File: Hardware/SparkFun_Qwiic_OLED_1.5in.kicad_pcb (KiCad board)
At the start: 2 copper layers, 34.3 x 48.3 mm, 72 parts, among them J1 Qwiic_RA, J2 Qwiic_RA, J4 Conn_01x24_FPC, J5 Conn_01x07, U2 WEO128128ASAP3N00000, U5 AP3012

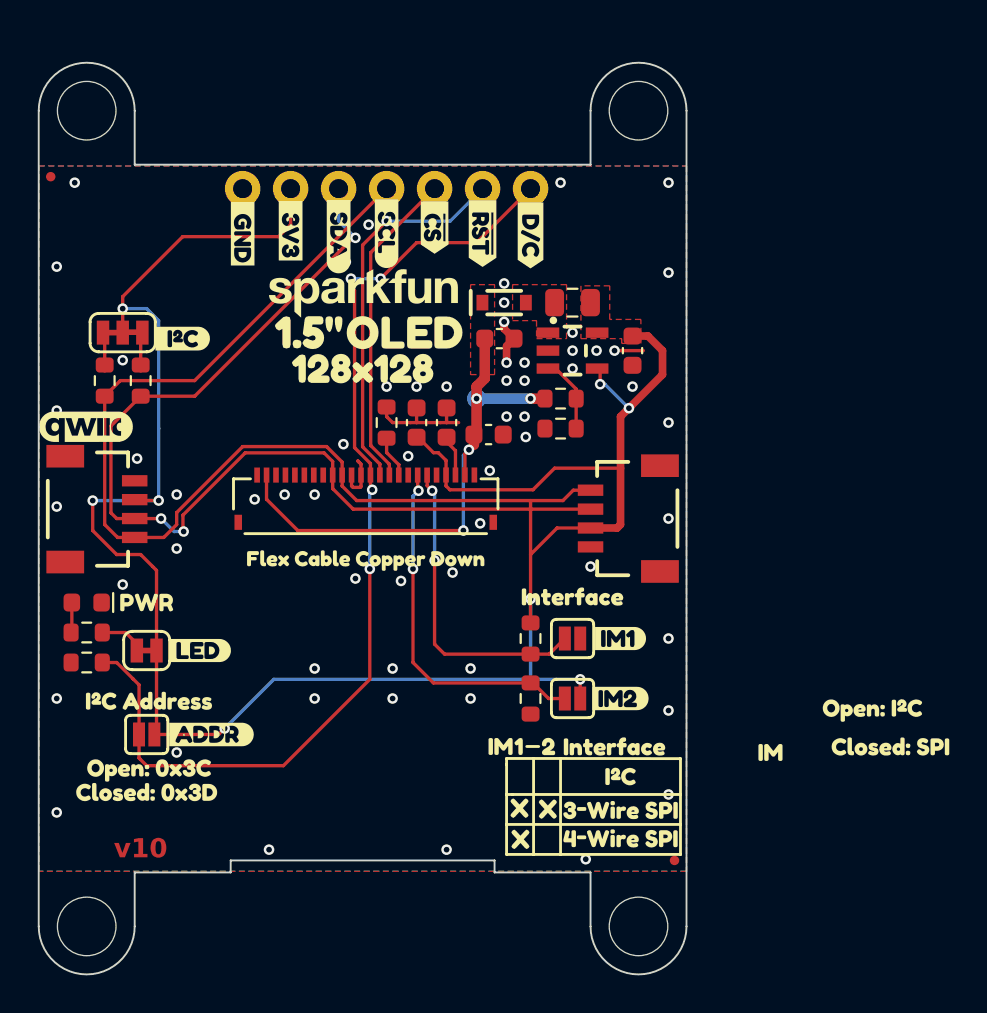
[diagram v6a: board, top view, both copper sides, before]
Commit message: Fixes the qwiic connectors being misaligned, updates measures
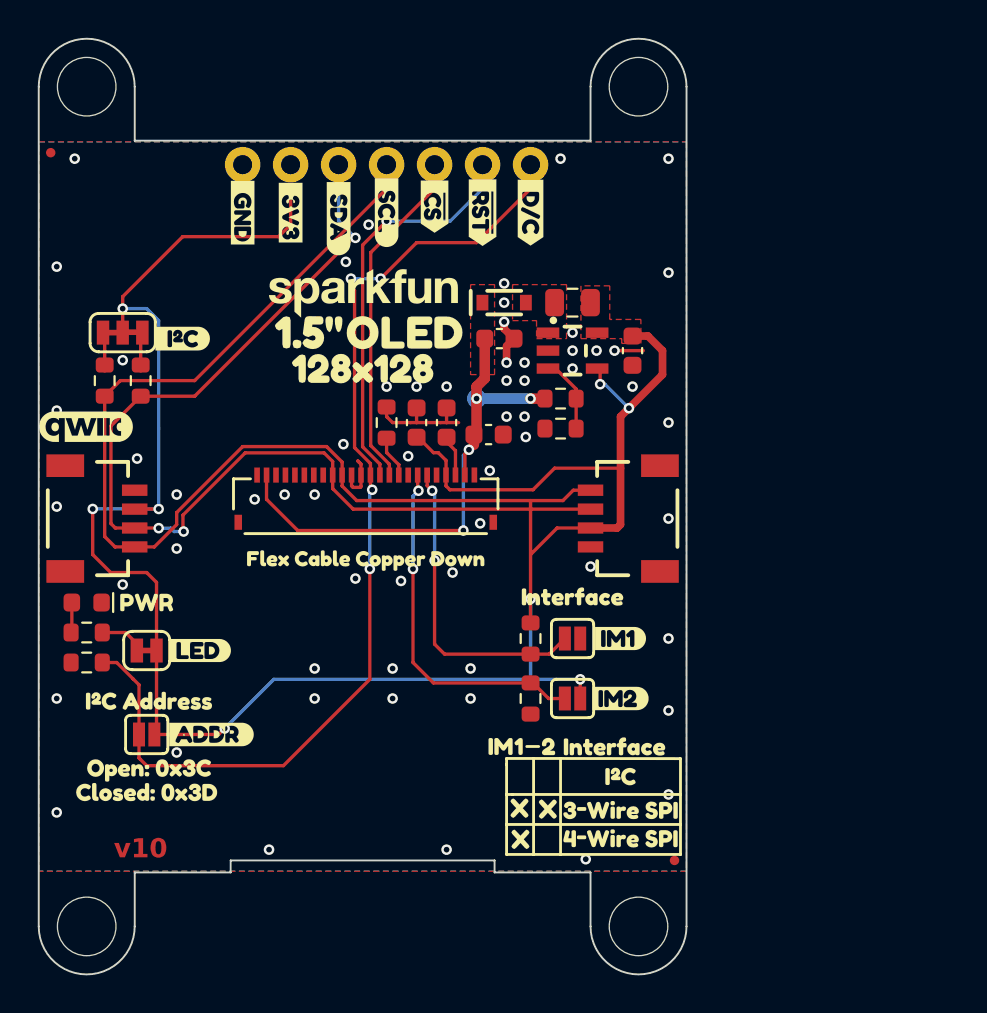
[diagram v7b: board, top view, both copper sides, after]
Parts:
- removed kibuzzard-680FCA02: G***, kibuzzard-680FCA02
- removed kibuzzard-680FCAD6: G***, kibuzzard-680FCAD6
- removed kibuzzard-68938227: G***, kibuzzard-68938227
- moved FID3 1.27 mm to (123.9, 67.3)
- moved J5 1.27 mm to (134.1, 67.9)
- moved ST1 1.27 mm to (125.8, 63.8)
- moved ST2 1.27 mm to (155.0, 63.8)
- moved kibuzzard-685B1775 1.21 mm to (149.3, 70.5)
- moved kibuzzard-67BF7EBF 1.11 mm to (134.1, 70.5)
- moved kibuzzard-67BF7F2F 1.11 mm to (141.7, 70.5)
- moved kibuzzard-680E7A4B 1.11 mm to (146.8, 70.5)
- moved kibuzzard-680E7A69 1.11 mm to (144.2, 70.2)
- moved kibuzzard-67BF7ED9 0.95 mm to (136.6, 70.5)
- moved kibuzzard-67BF7F13 0.95 mm to (139.1, 70.8)
- moved J2 0.50 mm to (128.3, 86.7)
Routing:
- net SCL/SCK: track 56.8 -> 57.6 mm
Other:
- board size 34.3 x 48.3 mm -> 34.3 x 49.5 mm

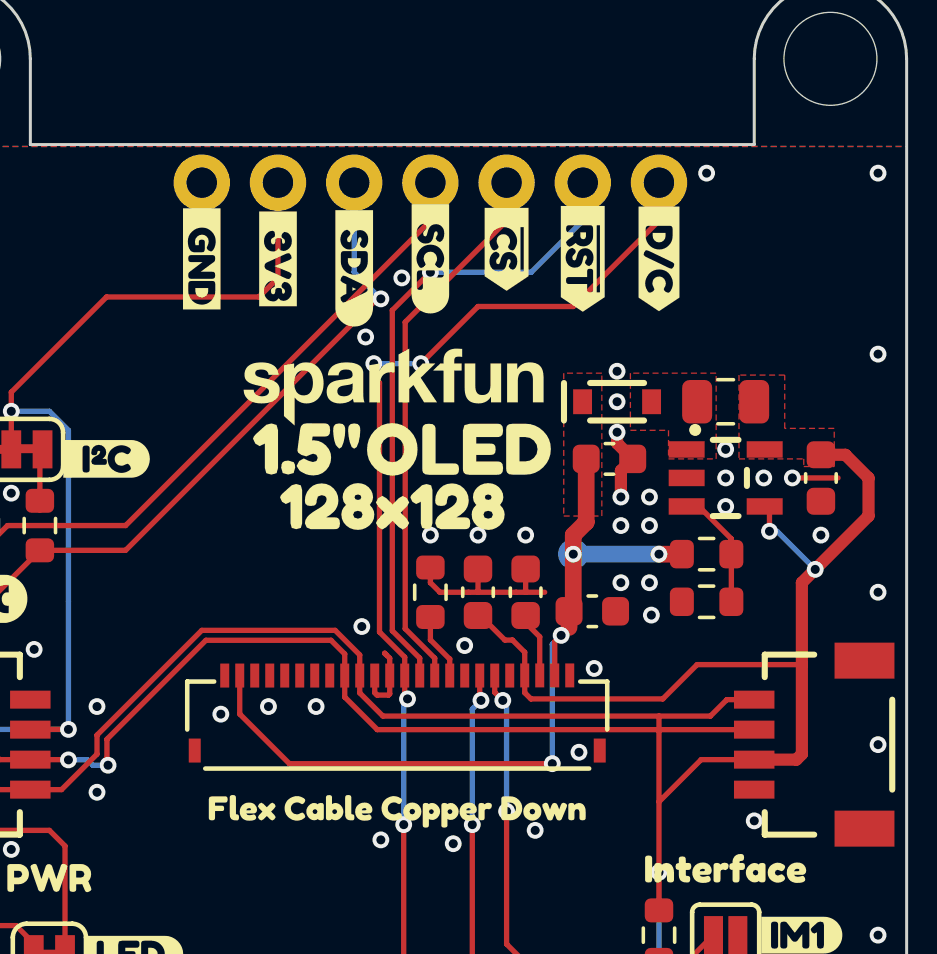
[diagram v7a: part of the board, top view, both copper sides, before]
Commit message: Increases the size of the board by .05", moves the FPC connector over .0065" so that it's in the center
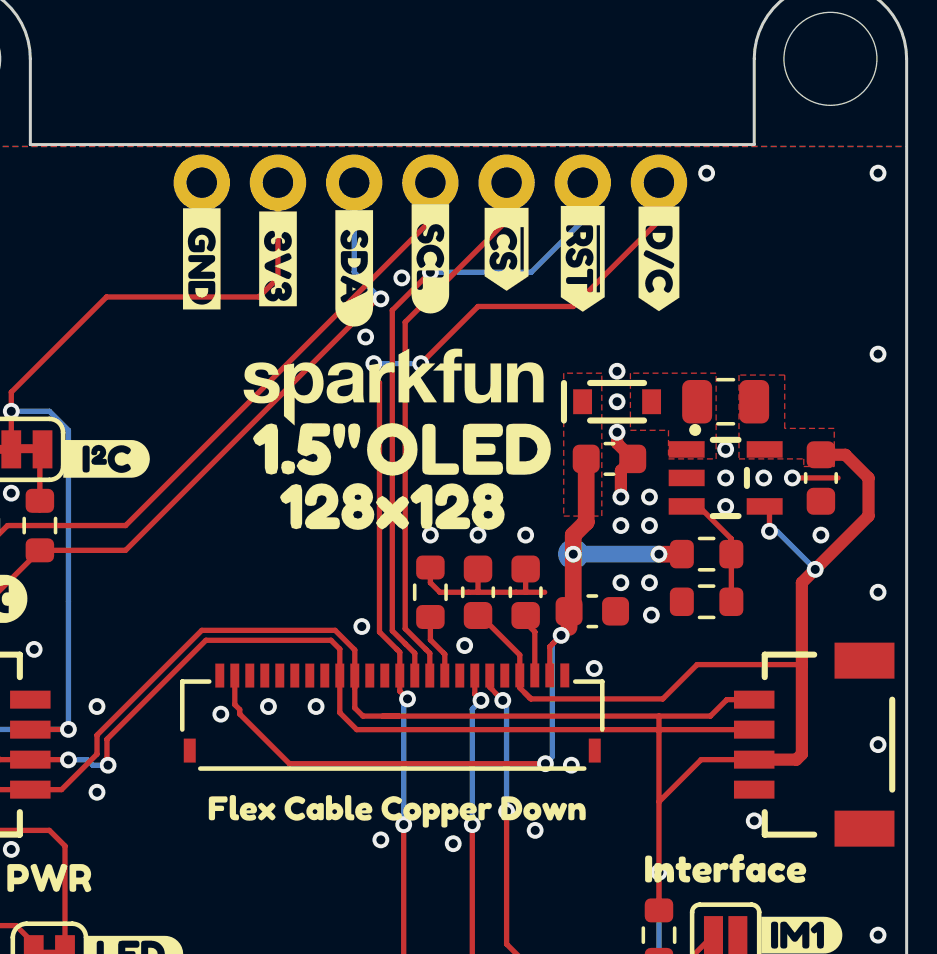
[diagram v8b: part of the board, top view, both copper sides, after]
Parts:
- moved U2 0.53 mm to (140.4, 87.4)
- moved J4 0.17 mm to (140.4, 85.7)
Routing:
- net GND: track 13.0 -> 10.1 mm
- net SCL/SCK: track 57.6 -> 59.7 mm
- net SDA/SDI: track 55.2 -> 56.9 mm
- net D/C: track 53.8 -> 55.2 mm
- net 3.3V: track 115.4 -> 116.7 mm
- net ~{RST}: track 20.1 -> 21.3 mm
- net ~{CS}: track 17.0 -> 18.2 mm
